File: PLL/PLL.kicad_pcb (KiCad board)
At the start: 2 copper layers, 100 x 200 mm, 4 parts, among them J1 EuroPower

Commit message: Starting the PLL
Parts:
- removed H3: Panel, Kosmo_panel:Kosmo_Panel_Dual_Mounting_Holes
- added C1: 10u, Capacitor_THT:CP_Radial_D8.0mm_P3.80mm, F.Cu at (83.0, 133.1)
- added C2: 100n, Capacitor_THT:C_Disc_D7.0mm_W2.5mm_P5.00mm, F.Cu at (101.2, 134.4)
- added C3: 100n, Capacitor_THT:C_Disc_D7.0mm_W2.5mm_P5.00mm, F.Cu at (81.7, 139.9)
- added C4: 100n, Capacitor_THT:C_Disc_D7.0mm_W2.5mm_P5.00mm, F.Cu at (101.2, 130.3)
- added C5: 100n, Capacitor_THT:C_Disc_D7.0mm_W2.5mm_P5.00mm, F.Cu at (90.3, 139.9)
- added C6: 10u, Capacitor_THT:CP_Radial_D8.0mm_P3.80mm, F.Cu at (92.7, 133.1)
- added D1: 1N4148, Diode_THT:D_DO-35_SOD27_P7.62mm_Horizontal, F.Cu at (72.9, 93.8)
- added D6: LED, LED_SMD:LED_1206_3216Metric_ReverseMount_Hole1.8x2.4mm, F.Cu at (89.0, 147.2)
- added J10: D8, telec:JackHole, F.Cu at (47.3, 28.8)
- added J2: Mix, telec:JackHole, F.Cu at (47.2, 175.1)
- added J3: M8, telec:JackHole, F.Cu at (47.2, 154.1)
- added J4: Clock, telec:JackHole, F.Cu at (47.2, 133.1)
- added J5: M4, telec:JackHole, F.Cu at (47.2, 112.1)
- added J6: M2, telec:JackHole, F.Cu at (47.2, 91.1)
- added J7: M1, telec:JackHole, F.Cu at (47.2, 70.1)
- added J8: D2, telec:JackHole, F.Cu at (47.2, 196.1)
- added J9: D4, telec:JackHole, F.Cu at (47.3, 49.8)
- added LOGO1: telec, logo:telec-8, F.Cu at (37.0, 16.3)
- added R1: 1k, Resistor_THT:R_Axial_DIN0204_L3.6mm_D1.6mm_P7.62mm_Horizontal, F.Cu at (83.6, 93.6)
- added R11: 1k, Resistor_SMD:R_1206_3216Metric_Pad1.42x1.75mm_HandSolder, F.Cu at (89.5, 143.6)
- added R12: 100k, Resistor_THT:R_Axial_DIN0204_L3.6mm_D1.6mm_P7.62mm_Horizontal, F.Cu at (93.9, 99.9)
- added R13: 100k, Resistor_THT:R_Axial_DIN0204_L3.6mm_D1.6mm_P7.62mm_Horizontal, F.Cu at (72.8, 103.0)
- added R14: 100k, Resistor_THT:R_Axial_DIN0204_L3.6mm_D1.6mm_P7.62mm_Horizontal, F.Cu at (83.4, 103.0)
- added R15: 100k, Resistor_THT:R_Axial_DIN0204_L3.6mm_D1.6mm_P7.62mm_Horizontal, F.Cu at (93.9, 103.0)
- added R16: 100k, Resistor_THT:R_Axial_DIN0204_L3.6mm_D1.6mm_P7.62mm_Horizontal, F.Cu at (72.8, 106.2)
- added R17: 100k, Resistor_THT:R_Axial_DIN0204_L3.6mm_D1.6mm_P7.62mm_Horizontal, F.Cu at (83.4, 106.2)
- added R18: 100k, Resistor_THT:R_Axial_DIN0204_L3.6mm_D1.6mm_P7.62mm_Horizontal, F.Cu at (72.8, 109.3)
- added R19: 100k, Resistor_THT:R_Axial_DIN0204_L3.6mm_D1.6mm_P7.62mm_Horizontal, F.Cu at (83.4, 109.3)
- added R2: 100k, Resistor_THT:R_Axial_DIN0204_L3.6mm_D1.6mm_P7.62mm_Horizontal, F.Cu at (94.1, 93.6)
- added R20: 1k, Resistor_THT:R_Axial_DIN0204_L3.6mm_D1.6mm_P7.62mm_Horizontal, F.Cu at (83.6, 96.8)
- added R21: 1k, Resistor_THT:R_Axial_DIN0204_L3.6mm_D1.6mm_P7.62mm_Horizontal, F.Cu at (83.4, 112.5)
- added R22: 1k, Resistor_THT:R_Axial_DIN0204_L3.6mm_D1.6mm_P7.62mm_Horizontal, F.Cu at (72.8, 115.7)
- added R23: 1k, Resistor_THT:R_Axial_DIN0204_L3.6mm_D1.6mm_P7.62mm_Horizontal, F.Cu at (72.8, 125.1)
- added R24: 1k, Resistor_THT:R_Axial_DIN0204_L3.6mm_D1.6mm_P7.62mm_Horizontal, F.Cu at (72.8, 122.0)
- added R25: 1k, Resistor_THT:R_Axial_DIN0204_L3.6mm_D1.6mm_P7.62mm_Horizontal, F.Cu at (72.8, 118.8)
- added R26: 1k, Resistor_THT:R_Axial_DIN0204_L3.6mm_D1.6mm_P7.62mm_Horizontal, F.Cu at (72.8, 112.5)
- added R3: 100k, Resistor_THT:R_Axial_DIN0204_L3.6mm_D1.6mm_P7.62mm_Horizontal, F.Cu at (104.7, 93.6)
- added R4: 10k, Resistor_THT:R_Axial_DIN0204_L3.6mm_D1.6mm_P7.62mm_Horizontal, F.Cu at (94.1, 96.8)
- added R5: 470k, Resistor_THT:R_Axial_DIN0204_L3.6mm_D1.6mm_P7.62mm_Horizontal, F.Cu at (72.8, 99.9)
- added R6: 470k, Resistor_THT:R_Axial_DIN0204_L3.6mm_D1.6mm_P7.62mm_Horizontal, F.Cu at (83.4, 99.9)
- added RV1: 100k, Potentiometer_THT:Potentiometer_Piher_T-16L_Single_Vertical_Hole, F.Cu at (16.6, 109.4)
- added RV2: 100k, Potentiometer_THT:Potentiometer_Piher_T-16L_Single_Vertical_Hole, F.Cu at (14.9, 183.7)
- added RV3: 100k, Potentiometer_THT:Potentiometer_Piher_T-16L_Single_Vertical_Hole, F.Cu at (15.0, 164.4)
- added RV4: 100k, Potentiometer_THT:Potentiometer_Piher_T-16L_Single_Vertical_Hole, F.Cu at (15.8, 128.4)
- added RV5: 100k, Potentiometer_THT:Potentiometer_Piher_T-16L_Single_Vertical_Hole, F.Cu at (14.9, 201.2)
- added RV6: 100k, Potentiometer_THT:Potentiometer_Piher_T-16L_Single_Vertical_Hole, F.Cu at (15.0, 146.9)
- added RV7: 100k, Potentiometer_THT:Potentiometer_Piher_T-16L_Single_Vertical_Hole, F.Cu at (17.4, 91.4)
- added U2: TL082, Package_DIP:DIP-8_W7.62mm_LongPads, F.Cu at (70.3, 130.4)
- H1, H2: value Panel -> Mounting_Holes
- moved H2 47.6 mm to (15.1, 209.1)
- moved H1 44.0 mm to (59.1, 209.1)
- moved J1 5.51 mm to (27.8, 30.1)
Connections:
- J1 pad 1: (no net) -> -12V
- J1 pad 2: (no net) -> GND
- J1 pad 3: (no net) -> +12V
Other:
- board size 100 x 200 mm -> 50 x 200 mm

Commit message: It fits !
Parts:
- removed the C6 at (92.7, 133.1)
- removed the J2 at (47.2, 175.1)
- added C5: 1u, Capacitor_THT:CP_Radial_D4.0mm_P1.50mm, F.Cu at (26.1, 30.6)
- added C7: 10u, Capacitor_THT:CP_Radial_D4.0mm_P1.50mm, F.Cu at (30.2, 31.2)
- added C8: 10u, Capacitor_THT:CP_Radial_D4.0mm_P1.50mm, B.Cu at (14.7, 54.4)
- added J10: Mix, telec:JackHole, F.Cu at (48.1, 54.6)
- added SW1: Freq range, telec:SW_L13.2mm_W7.9mm_P4.7mm, F.Cu at (18.2, 34.3)
- added U2: CD4046, Package_DIP:DIP-16_W7.62mm_LongPads, F.Cu at (18.3, 50.7)
- added U3: CD4040, Package_DIP:DIP-16_W7.62mm_LongPads, F.Cu at (18.3, 64.4)
- D1: footprint Diode_THT:D_DO-35_SOD27_P7.62mm_Horizontal -> Diode_SMD:D_1206_3216Metric_Pad1.42x1.75mm_HandSolder
- D2: renamed from D6; moved to B.Cu
- R1: renamed from R2; footprint Resistor_THT:R_Axial_DIN0204_L3.6mm_D1.6mm_P7.62mm_Horizontal -> Resistor_SMD:R_1206_3216Metric_Pad1.42x1.75mm_HandSolder
- R14: renamed from R19; footprint Resistor_THT:R_Axial_DIN0204_L3.6mm_D1.6mm_P7.62mm_Horizontal -> Resistor_SMD:R_1206_3216Metric_Pad1.42x1.75mm_HandSolder
- R15: renamed from R1; footprint Resistor_THT:R_Axial_DIN0204_L3.6mm_D1.6mm_P7.62mm_Horizontal -> Resistor_SMD:R_1206_3216Metric_Pad1.42x1.75mm_HandSolder
- R2: renamed from R3; footprint Resistor_THT:R_Axial_DIN0204_L3.6mm_D1.6mm_P7.62mm_Horizontal -> Resistor_SMD:R_1206_3216Metric_Pad1.42x1.75mm_HandSolder
- R6: renamed from R11; moved to B.Cu
- U1: renamed from U2; footprint Package_DIP:DIP-8_W7.62mm_LongPads -> Package_SO:SOIC-8_3.9x4.9mm_P1.27mm
- moved J9 165.8 mm to (48.2, 194.6), turned to 90 degrees
- moved J8 124.8 mm to (48.2, 174.6), turned to 90 degrees
- moved C2 117.7 mm to (15.2, 49.2), turned to 90 degrees
- moved RV7 113.9 mm to (30.4, 204.6), turned to 90 degrees
- moved C6 113.7 mm to (36.3, 35.7), turned to 180 degrees
- moved C3 111.8 mm to (68.3, 22.3), turned to 90 degrees
- moved U1 111.6 mm to (52.0, 20.3), turned to 90 degrees
- moved C1 109.2 mm to (15.2, 63.1), turned to 90 degrees
- moved C4 104.6 mm to (34.7, 53.7), turned to 180 degrees
- moved R13 102.7 mm to (16.0, 194.9), turned to 90 degrees
- moved RV1 100.3 mm to (30.4, 84.6), turned to 90 degrees
- moved R14 99.4 mm to (51.9, 15.1)
- moved J1 98.5 mm to (48.2, 34.6), turned to 90 degrees
- moved R22 96.9 mm to (42.2, 204.4), turned to 180 degrees
- moved R12 96.3 mm to (15.9, 174.9), turned to 90 degrees
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- renumbered C4 to C1, C5 to C2, C1 to C3, C2 to C4, C3 to C6, J4 to J1, J1 to J2, J5 to J4, J6 to J5, J7 to J6, J8 to J7, J9 to J8, J10 to J9, R15 to R10, R16 to R11, R17 to R12, R18 to R13, R20 to R16, R21 to R17, R22 to R18, R23 to R19, R24 to R20, R25 to R21, R26 to R22, R4 to R3, R5 to R4, R6 to R5, R12 to R7, R13 to R8, R14 to R9, RV2 to RV1, RV1 to RV2
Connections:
- C2 pad 2: -12V -> +12V
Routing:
- net /D8: track 0.00 -> 158.7 mm
- net Net-(C8-Pad1): track 0.00 -> 147.6 mm
- net /D4: track 0.00 -> 130.8 mm
- net /D2: track 0.00 -> 110.9 mm
- net /M1: track 0.00 -> 106.3 mm
- net /M2: track 0.00 -> 73.0 mm
- net /M4: track 0.00 -> 54.0 mm
- net Net-(J9-PadT): track 0.00 -> 34.2 mm
- net Net-(J8-PadT): track 0.00 -> 34.1 mm
- net Net-(J7-PadT): track 0.00 -> 34.1 mm
- net Net-(J5-PadT): track 0.00 -> 34.1 mm
- net Net-(J4-PadT): track 0.00 -> 34.1 mm
- net Net-(J3-PadT): track 0.00 -> 34.1 mm
- net Net-(J6-PadT): track 0.00 -> 34.1 mm
- net /M8: track 0.00 -> 28.0 mm
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- added copper zone on B.Cu, net GND

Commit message: PLL layout done
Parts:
- removed the R17 at (42.2, 104.3)
- added C10: 1u, Capacitor_THT:CP_Radial_D4.0mm_P1.50mm, B.Cu at (35.2, 121.7)
- added C11: 1u, Capacitor_THT:CP_Radial_D4.0mm_P1.50mm, B.Cu at (35.2, 141.8)
- added C12: 1u, Capacitor_THT:CP_Radial_D4.0mm_P1.50mm, B.Cu at (35.2, 161.7)
- added C13: 1u, Capacitor_THT:CP_Radial_D4.0mm_P1.50mm, B.Cu at (35.2, 181.7)
- added C14: 1u, Capacitor_THT:CP_Radial_D4.0mm_P1.50mm, B.Cu at (35.2, 201.8)
- added C9: 1u, Capacitor_THT:CP_Radial_D4.0mm_P1.50mm, B.Cu at (35.2, 101.7)
- added D2: LED, LED_SMD:LED_1206_3216Metric_ReverseMount_Hole1.8x2.4mm, B.Cu at (59.0, 42.9)
- added D3: LED, LED_SMD:LED_1206_3216Metric_ReverseMount_Hole1.8x2.4mm, B.Cu at (59.0, 82.9)
- added D4: LED, LED_SMD:LED_1206_3216Metric_ReverseMount_Hole1.8x2.4mm, B.Cu at (59.0, 102.9)
- added D5: LED, LED_SMD:LED_1206_3216Metric_ReverseMount_Hole1.8x2.4mm, B.Cu at (59.0, 122.9)
- added D6: LED, LED_SMD:LED_1206_3216Metric_ReverseMount_Hole1.8x2.4mm, B.Cu at (59.0, 142.9)
- added D7: LED, LED_SMD:LED_1206_3216Metric_ReverseMount_Hole1.8x2.4mm, B.Cu at (59.0, 163.0)
- added D8: LED, LED_SMD:LED_1206_3216Metric_ReverseMount_Hole1.8x2.4mm, B.Cu at (59.0, 183.0)
- added R10: 1k, Resistor_SMD:R_1206_3216Metric_Pad1.42x1.75mm_HandSolder, B.Cu at (54.1, 142.8)
- added R11: 1k, Resistor_SMD:R_1206_3216Metric_Pad1.42x1.75mm_HandSolder, B.Cu at (54.1, 162.8)
- added R12: 1k, Resistor_SMD:R_1206_3216Metric_Pad1.42x1.75mm_HandSolder, B.Cu at (54.1, 182.8)
- added R14: 470k, Resistor_THT:R_Axial_DIN0204_L3.6mm_D1.6mm_P7.62mm_Horizontal, F.Cu at (36.5, 37.4)
- added R26: 1k, Resistor_THT:R_Axial_DIN0204_L3.6mm_D1.6mm_P7.62mm_Horizontal, F.Cu at (42.3, 104.3)
- added R3: 100k, Resistor_SMD:R_1206_3216Metric_Pad1.42x1.75mm_HandSolder, F.Cu at (36.9, 33.2)
- added R4: 100k, Resistor_SMD:R_1206_3216Metric_Pad1.42x1.75mm_HandSolder, F.Cu at (34.6, 33.2)
- added R6: 1k, Resistor_SMD:R_1206_3216Metric_Pad1.42x1.75mm_HandSolder, B.Cu at (54.1, 82.8)
- added R8: 1k, Resistor_SMD:R_1206_3216Metric_Pad1.42x1.75mm_HandSolder, B.Cu at (54.1, 102.8)
- added R9: 1k, Resistor_SMD:R_1206_3216Metric_Pad1.42x1.75mm_HandSolder, B.Cu at (54.1, 122.8)
- C3: footprint Capacitor_THT:CP_Radial_D8.0mm_P3.80mm -> Capacitor_THT:CP_Radial_D4.0mm_P1.50mm; moved to B.Cu
- C8: value 10u -> 1u
- R1, R2: moved to B.Cu
- R5: value 470k -> 1k; footprint Resistor_THT:R_Axial_DIN0204_L3.6mm_D1.6mm_P7.62mm_Horizontal -> Resistor_SMD:R_1206_3216Metric_Pad1.42x1.75mm_HandSolder; moved to B.Cu
- moved R24 36.3 mm to (34.3, 19.5), turned to 180 degrees
- moved C8 34.1 mm to (35.2, 81.7)
- moved C3 28.8 mm to (39.5, 23.8)
- moved R1 22.6 mm to (36.9, 33.2)
- moved D9 19.9 mm to (59.0, 202.9)
- moved R15 19.9 mm to (54.1, 202.9)
- moved U1 19.0 mm to (34.2, 26.9)
- moved R23 18.9 mm to (34.3, 21.9)
- moved R5 18.2 mm to (54.2, 42.9), turned to 0 degrees
- moved R2 17.7 mm to (34.6, 33.2), turned to 90 degrees
- moved D1 17.7 mm to (32.3, 33.2), turned to 90 degrees
- moved C7 9.54 mm to (24.7, 39.0), turned to 90 degrees
- moved LOGO1 8.52 mm to (48.2, 18.1)
- moved C6 7.83 mm to (28.6, 34.3)
- moved C5 1.72 mm to (24.7, 29.6)
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- renumbered D2 to D9, R4 to R13, R6 to R15, R7 to R16, R8 to R17, R9 to R18, R10 to R19, R11 to R20, R12 to R21, R13 to R22, R14 to R23, R15 to R24, R16 to R25, R18 to R27, R19 to R28, R20 to R29, R21 to R30, R22 to R31, R3 to R7
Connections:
- C8 pad 1: Net-(C8-Pad1) -> /D8
- R1 pad 1: GND -> +12V
- R13 pad 2: Net-(R4-Pad2) -> Net-(R13-Pad2)
- R15 pad 1: /Clk -> /M8
- R16 pad 2: Net-(C8-Pad1) -> Net-(R16-Pad2)
- R17 pad 2: Net-(C8-Pad1) -> Net-(R16-Pad2)
- R18 pad 2: Net-(C8-Pad1) -> Net-(R16-Pad2)
- R19 pad 2: Net-(C8-Pad1) -> Net-(R16-Pad2)
- R2 pad 2: /Clk_in -> GND
- R20 pad 2: Net-(C8-Pad1) -> Net-(R16-Pad2)
- R21 pad 2: Net-(C8-Pad1) -> Net-(R16-Pad2)
- R22 pad 2: Net-(C8-Pad1) -> Net-(R16-Pad2)
- R23 pad 2: Net-(C8-Pad2) -> Net-(R16-Pad2)
- R25 pad 2: /M8 -> /D8
- R27 pad 2: /M2 -> /D2
- R29 pad 2: /D2 -> /M2
- R30 pad 2: /D4 -> /M4
- R31 pad 2: /D8 -> /M8
- R5 pad 1: Net-(R4-Pad2) -> /Clk_in
- R5 pad 2: Net-(C6-Pad2) -> Net-(D2-Pad2)
- RV1 pad 1: /M8 -> Net-(C8-Pad2)
- RV2 pad 1: /M4 -> Net-(C9-Pad2)
- RV3 pad 1: /M2 -> Net-(C10-Pad2)
- RV4 pad 1: /M1 -> Net-(C11-Pad2)
- RV5 pad 1: /D2 -> Net-(C12-Pad2)
- RV6 pad 1: /D4 -> Net-(C13-Pad2)
- RV7 pad 1: /D8 -> Net-(C14-Pad2)
- U1 pad 3: Net-(R1-Pad2) -> Net-(R3-Pad2)
- U1 pad 6: Net-(C8-Pad2) -> Net-(R16-Pad2)
- U2 pad 9: Net-(R4-Pad2) -> Net-(R13-Pad2)
- U3 pad 2: /M4 -> /D4
- U3 pad 3: /M2 -> /D2
- U3 pad 4: /M8 -> /D8
- U3 pad 6: /D2 -> /M2
- U3 pad 7: /D4 -> /M4
- U3 pad 9: /D8 -> /M8
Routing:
- net Net-(R16-Pad2): track 0.00 -> 208.4 mm, vias 0 -> 2
- net /M8: track 28.0 -> 175.8 mm
- net Net-(C8-Pad1): track 147.6 -> 0.00 mm
- net /D8: track 158.7 -> 46.4 mm
- net /M4: track 54.0 -> 147.9 mm
- net +12V: track 22.1 -> 86.9 mm
- net /D4: track 130.8 -> 74.0 mm
- net /M2: track 73.0 -> 128.0 mm
- net /Clk_in: track 0.00 -> 51.7 mm, vias 0 -> 1
- net Net-(J10-PadT): track 0.00 -> 48.3 mm
- net /IN: track 0.00 -> 28.3 mm, vias 0 -> 2
- net /D2: track 110.9 -> 91.6 mm
- net /M1: track 106.3 -> 124.0 mm
- net -12V: track 0.00 -> 12.9 mm
- net Net-(C6-Pad2): track 0.00 -> 12.1 mm
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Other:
- board text added: "Mixed PLL"
- board text added: "Schematic from BMC33. 4046 Wave Shaper"

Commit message: PLL done !
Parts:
- J3: value M8 -> D8
- J4: value M4 -> D4
- J5: value M2 -> D2
- J7: value D2 -> M2
- J8: value D4 -> M4
- J9: value D8 -> M8
- moved C6 1.10 mm to (29.7, 34.3)
- moved C5 0.70 mm to (25.4, 29.6)
- moved C7 0.70 mm to (25.4, 39.0)
- moved SW1 0.70 mm to (18.8, 34.3)
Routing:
- net Net-(C6-Pad2): track 12.1 -> 11.4 mm
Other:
- board text added: "+"
- board text added: "-"
- board text added: "1:1"
- board text added: "1:2"
- board text added: "1:4"
- board text added: "1:8"
- board text added: "2:1"
- board text added: "4:1"
- board text added: "8:1"
- board text added: "CLK"
- board text added: "D2"
- board text added: "D4"
- board text added: "D8"
- board text added: "M1"
- board text added: "M2"
- board text added: "M4"
- board text added: "M8"
- board text added: "MIX"

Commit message: Added PCB ref stamp and send to prod!
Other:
- board text added: "PCB ref here:"
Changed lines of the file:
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@@
   (general
     (thickness 1.6)
-    (drawings 91)
+    (drawings 96)
     (tracks 319)
     (zones 0)
@@
       (net 2 +12V))
   )
+  (gr_text "PCB ref here:" (at 26.6 59.3) (layer F.SilkS)
+    (effects (font (size 1 1) (thickness 0.15)))
+  )
+  (gr_line (start 19.5 62.8) (end 19.5 58.5) (layer F.SilkS) (width 0.15))
+  (gr_line (start 34.5 62.8) (end 19.5 62.8) (layer F.SilkS) (width 0.15))
+  (gr_line (start 34.5 58.5) (end 34.5 62.8) (layer F.SilkS) (width 0.15))
+  (gr_line (start 19.5 58.5) (end 34.5 58.5) (layer F.SilkS) (width 0.15))
   (gr_text - (at 13.7 29.5) (layer F.SilkS)
     (effects (font (size 2 2) (thickness 0.3)))

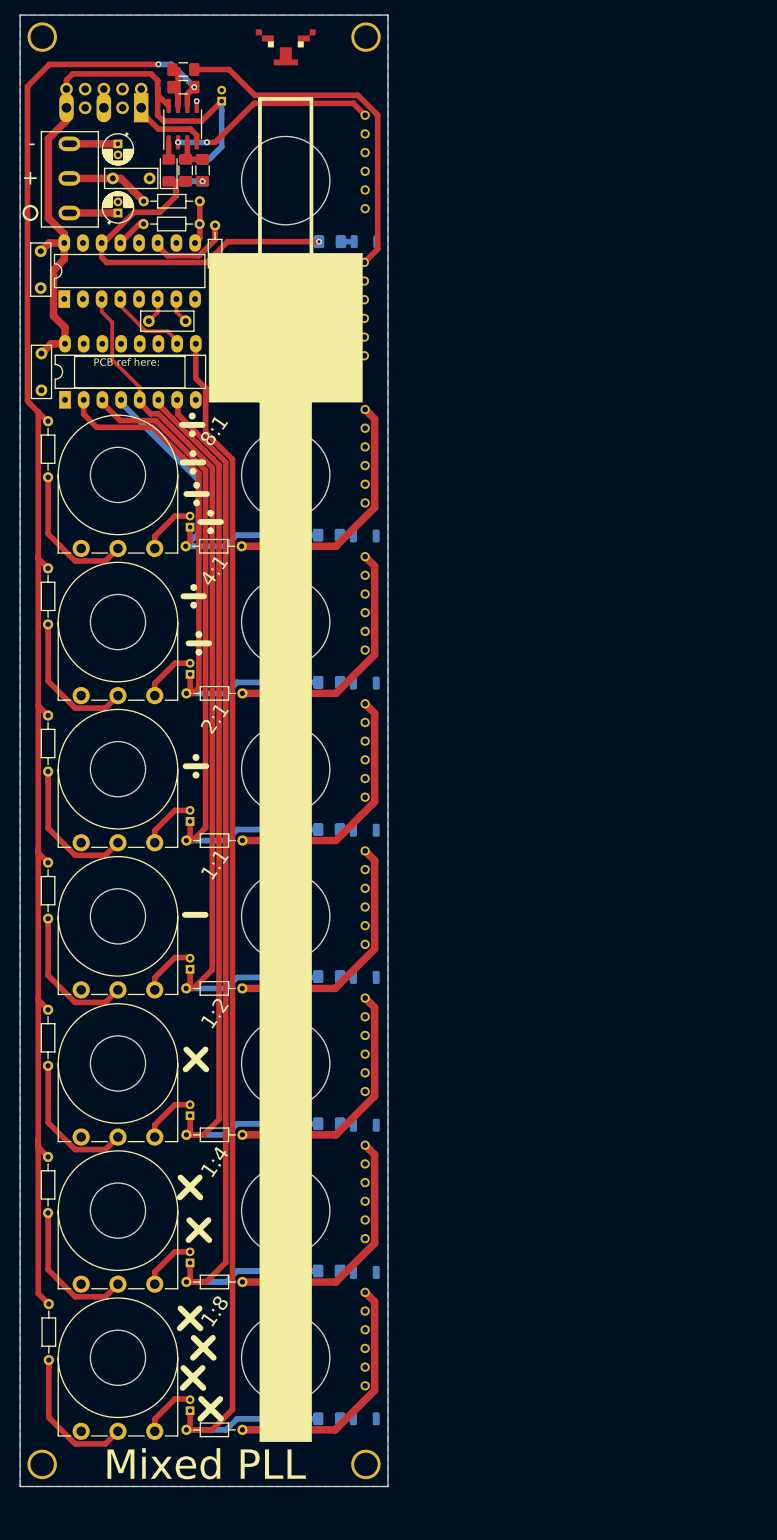
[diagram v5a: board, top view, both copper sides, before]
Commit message: Started PLL layout
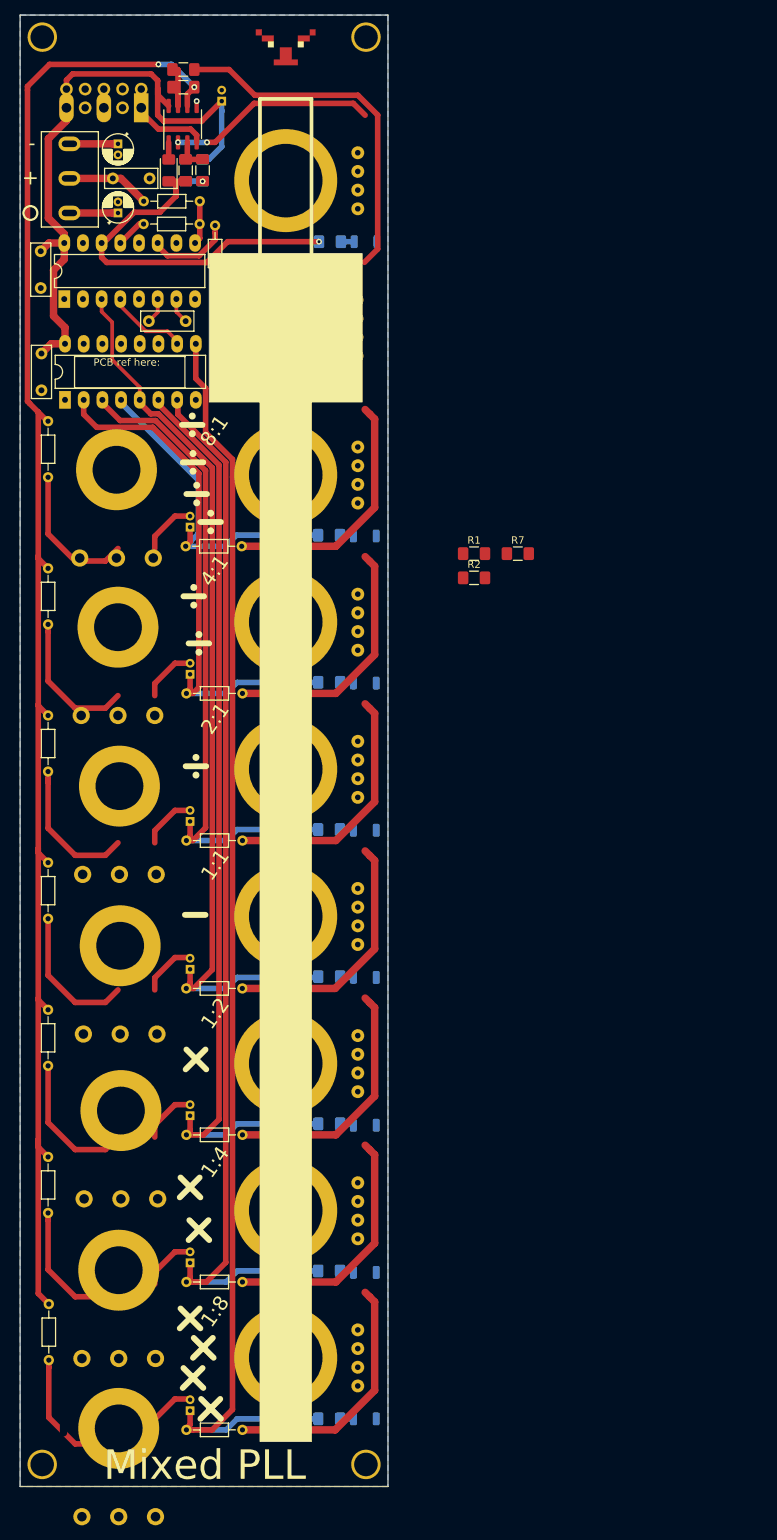
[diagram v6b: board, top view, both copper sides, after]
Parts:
- added R1: 100k, Resistor_SMD:R_1206_3216Metric_Pad1.42x1.75mm_HandSolder, F.Cu at (73.8, 85.3)
- added R2: 2k7, Resistor_SMD:R_1206_3216Metric_Pad1.42x1.75mm_HandSolder, F.Cu at (73.8, 88.6)
- added R7: 100k, Resistor_SMD:R_1206_3216Metric_Pad1.42x1.75mm_HandSolder, F.Cu at (79.8, 85.3)
- C2: renamed from C4; value 100n -> 1n
- J1, J10, J3, J4, J5, J6, J7, J8, J9: footprint telec:JackHole -> telec:Jack_Hole_Square
- R10: renamed from R6; value 1k -> 2k7
- R11: renamed from R8; value 1k -> 2k7
- R12: renamed from R9; value 1k -> 2k7
- R13: renamed from R10; value 1k -> 2k7
- R14: renamed from R11; value 1k -> 2k7
- R17: renamed from R12; value 1k -> 2k7
- R18: renamed from R15; value 1k -> 2k7
- R4: renamed from R2; value 100k -> 22k
- R5: renamed from R3; value 100k -> 10k
- R6: renamed from R4; value 100k -> 470k
- R8: renamed from R5; value 1k -> 2k7
- RV1, RV2, RV3, RV4, RV5, RV6, RV7: footprint Potentiometer_THT:Potentiometer_Piher_T-16L_Single_Vertical_Hole -> telec:Potentiometer_Single_Vertical_Hole
- SW1: value Freq range -> Lock speed
- moved RV1 11.9 mm to (25.2, 73.9), turned to 0 degrees
- moved RV2 10.6 mm to (25.4, 95.3), turned to 0 degrees
- moved RV3 9.07 mm to (25.6, 116.9), turned to 0 degrees
- moved RV4 7.62 mm to (25.7, 138.6), turned to 0 degrees
- moved RV5 5.84 mm to (25.8, 161.0), turned to 0 degrees
- moved RV6 5.26 mm to (25.5, 182.7), turned to 0 degrees
- moved RV7 4.92 mm to (25.5, 204.2), turned to 0 degrees
- renumbered C3 to C1, C1 to C3, C5 to C4, C6 to C5, C7 to C6, C2 to C7, R13 to R15, R14 to R16, R16 to R19, R17 to R20, R18 to R21, R19 to R22, R20 to R23, R21 to R24, R22 to R25, R23 to R26, R24 to R27, R25 to R28, R26 to R29, R1 to R3, R27 to R30, R28 to R31, R29 to R32, R30 to R33, R31 to R34, R7 to R9
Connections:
- D1 pad 2: Net-(D1-Pad2) -> /Trig
- D2 pad 1: GND -> Net-(D2-Pad1)
- D2 pad 2: Net-(D2-Pad2) -> GND
- J1 pad R: Net-(J1-PadR) -> /Reset
- R6 pad 2: /Clk_in -> /Trig
- R8 pad 1: /Clk_in -> /Trig
- R8 pad 2: Net-(D2-Pad2) -> Net-(D2-Pad1)
- U1 pad 1: Net-(D1-Pad2) -> /Trig
- U2 pad 5: GND -> /Reset
- U3 pad 11: GND -> /Reset
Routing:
- net Net-(R21-Pad1): track 19.9 -> 39.4 mm
- net Net-(R24-Pad1): track 19.4 -> 0.00 mm
- net Net-(R23-Pad1): track 19.4 -> 0.00 mm
- net Net-(R20-Pad1): track 19.4 -> 38.9 mm
- net Net-(R19-Pad1): track 19.4 -> 0.00 mm
- net Net-(R16-Pad1): track 0.00 -> 19.4 mm
- net Net-(R22-Pad1): track 19.4 -> 38.8 mm
- net Net-(R25-Pad1): track 19.4 -> 0.00 mm
- net Net-(D1-Pad2): track 2.33 -> 0.00 mm
- net /Trig: track 0.00 -> 2.33 mm
